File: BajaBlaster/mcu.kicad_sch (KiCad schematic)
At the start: 15 parts, among them J1 Conn_01x06_Socket, SW1 SW_Push, SW2 SW_Push, U1 ESP32-WROOM-32, U2 MPU-6050

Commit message: fixed one typographical error
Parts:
- C11: value .1uf -> 0.1uf
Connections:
- net CAN_RX: now also U1.10 (IO25); no longer U1.11 (IO26)
- net CAN_TX: now also U1.11 (IO26); no longer U1.10 (IO25)
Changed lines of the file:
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@@
 	(wire
 		(pts
-			(xy 83.82 88.9) (xy 80.01 88.9)
+			(xy 85.09 88.9) (xy 80.01 88.9)
 		)
 		(stroke
@@
 	(wire
 		(pts
-			(xy 83.82 86.36) (xy 80.01 86.36)
+			(xy 85.09 86.36) (xy 80.01 86.36)
 		)
 		(stroke
@@
 		)
 	)
-	(label "CAN_RX"
-		(at 83.82 88.9 0)
-		(effects
-			(font
-				(size 1.27 1.27)
-			)
-			(justify left bottom)
-		)
-	)
-	(label "CAN_TX"
-		(at 83.82 86.36 0)
-		(effects
-			(font
-				(size 1.27 1.27)
-			)
-			(justify left bottom)
-		)
-	)
 	(label "IMU_SDA"
 		(at 120.65 64.77 180)
@@
 		)
 	)
+	(hierarchical_label "CAN_TX"
+		(shape bidirectional)
+		(at 85.09 88.9 0)
+		(effects
+			(font
+				(size 1.27 1.27)
+			)
+			(justify left)
+		)
+	)
 	(hierarchical_label "IO1"
 		(shape bidirectional)
@@
 			)
 			(justify right)
+		)
+	)
+	(hierarchical_label "CAN_RX"
+		(shape bidirectional)
+		(at 85.09 86.36 0)
+		(effects
+			(font
+				(size 1.27 1.27)
+			)
+			(justify left)
 		)
 	)
@@
 			)
 		)
-		(property "Value" ".1uf"
+		(property "Value" "0.1uf"
 			(at 147.32 43.18 90)
 			(show_name no)

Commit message: doing lots of small tweaks and fixups
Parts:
- added R302: 50OHM, symbol Device:R
- C301: renamed from C6; value 1uf -> 1uF
- C302: renamed from C8; value 10uf -> 10uF
- C304: renamed from C11; value 0.1uf -> 0.1uF
- R303: renamed from R1; value 10k Ohm -> 10kOhm
- R304: renamed from R2; value 4.7k -> 4.7kOHM
- R305: renamed from R3; value 4.7k -> 4.7kOHM
- renumbered C7 to C303, C9 to C305, C10 to C306, J1 to J301, R4 to R301, SW1 to SW301, SW2 to SW302, U1 to U301, U2 to U302
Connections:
- net +3V3: now also R303.1; no longer R303.2
- net ESP32 EN: no longer C301.1, R301.2, SW301.1, U301.3 (EN)
- net IMU_SCL: no longer R305.1, U302.23 (SCL)
- net IMU_SDA: no longer R304.1, U302.24 (SDA)
- net IO0: now also R303.2; no longer R303.1
- net IO1: no longer U301.35 (TXD0/IO1)
- net IO3: no longer U301.34 (RXD0/IO3)
- net SYNC: now also R302.2; no longer U301.12 (IO27)
- new net: R304.1, U302.23 (SCL)
- new net: R305.1, U302.24 (SDA)
- new net: R302.1, U301.12 (IO27)
- new net ESP32_EN: C301.1, R301.2, SW301.1, U301.3 (EN)
- new net U0RXD: U301.34 (RXD0/IO3)
- new net U0TXD: U301.35 (TXD0/IO1)
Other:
- note added: "ACCELEROMETER UNIT"
- note added: "ESP32"
- note added: "TESTING PADS"
- title: (none) -> MCU_REV_A
- moved on the sheet: C301, C302, C303, C304, C305, C306, J301, R301, R303, R304, R305, SW301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

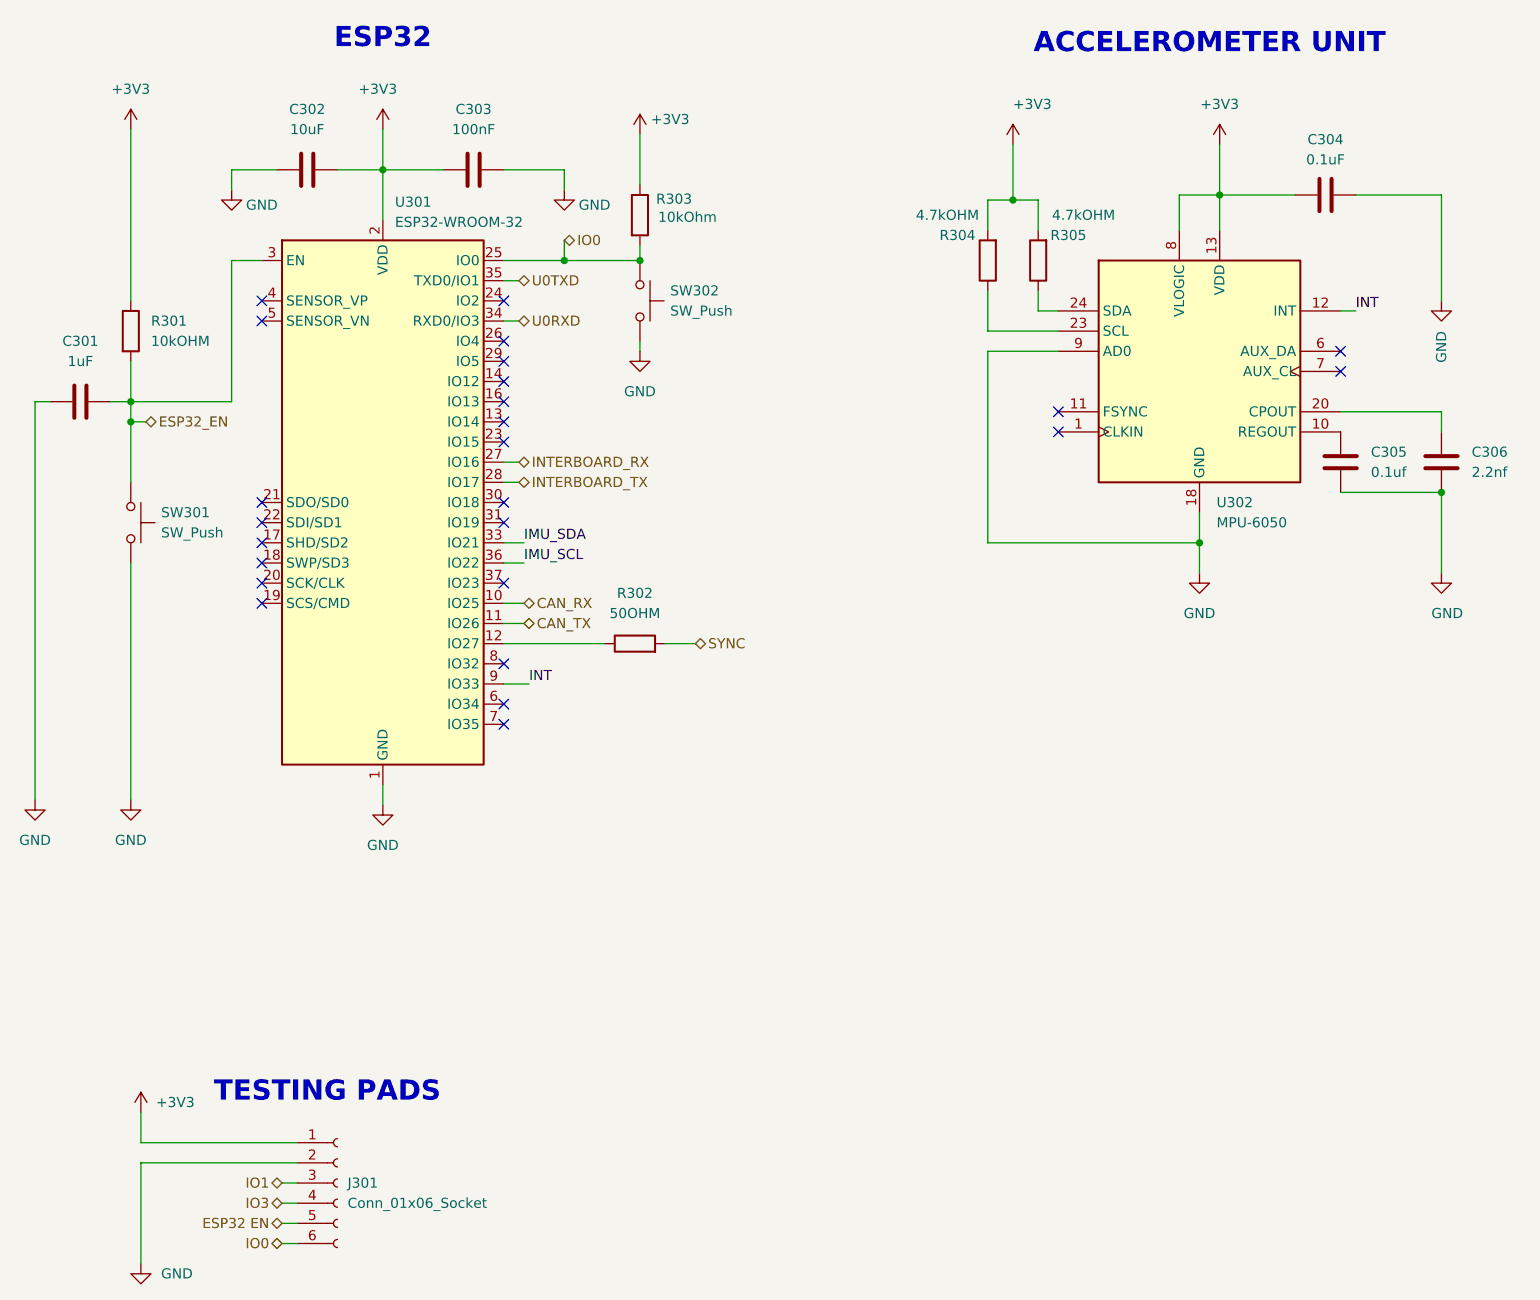
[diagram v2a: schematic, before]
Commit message: added better formatting across schematic
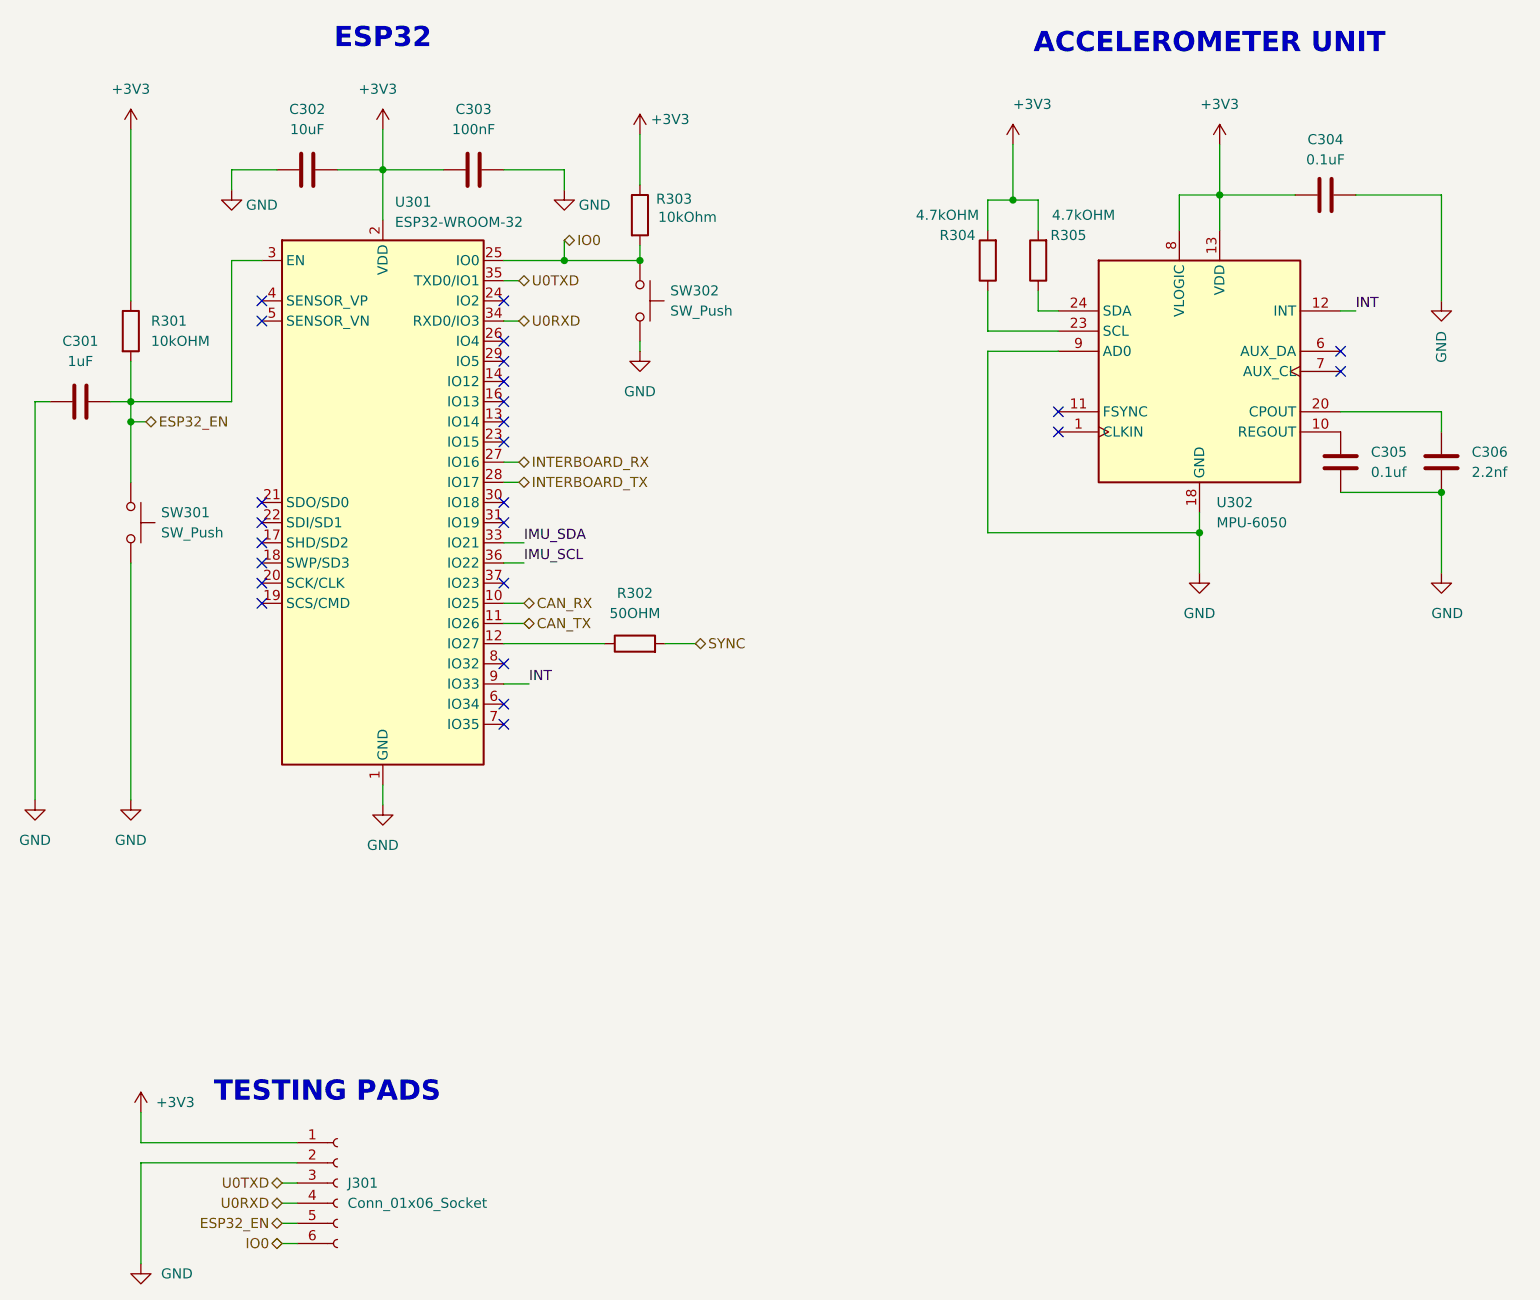
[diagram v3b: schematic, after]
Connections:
- net ESP32 EN is gone; now on net ESP32_EN: J301.5 (Pin_5)
- net IO1 is gone; now on net U0TXD: J301.3 (Pin_3)
- net IO3 is gone; now on net U0RXD: J301.4 (Pin_4)
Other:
- company: (none) -> Olin Baja SAE
- title: MCU_REV_A -> BAJA_BLASTER
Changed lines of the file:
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@@
 	(paper "A4")
 	(title_block
-		(title "MCU_REV_A")
+		(title "BAJA_BLASTER")
+		(date "2026-09-24")
+		(rev "A")
+		(company "Olin Baja SAE")
 	)
 	(text "ACCELEROMETER UNIT"
@@
 	)
 	(junction
-		(at 168.91 87.63)
-		(diameter 0)
-		(color 0 0 0 0)
-	)
-	(junction
 		(at 88.9 52.07)
 		(diameter 0)
@@
 	)
 	(junction
+		(at 168.91 86.36)
+		(diameter 0)
+		(color 0 0 0 0)
+	)
+	(junction
 		(at 34.29 72.39)
 		(diameter 0)
@@
 	(wire
 		(pts
-			(xy 168.91 83.82) (xy 168.91 87.63)
+			(xy 168.91 83.82) (xy 168.91 86.36)
 		)
 		(stroke
@@
 	(wire
 		(pts
+			(xy 168.91 86.36) (xy 168.91 91.44)
+		)
+		(stroke
+			(width 0)
+			(type default)
+		)
+	)
+	(wire
+		(pts
 			(xy 35.56 163.195) (xy 55.245 163.195)
 		)
@@
 	(wire
 		(pts
-			(xy 142.24 63.5) (xy 142.24 87.63)
-		)
-		(stroke
-			(width 0)
-			(type default)
-		)
-	)
-	(wire
-		(pts
-			(xy 142.24 87.63) (xy 168.91 87.63)
+			(xy 142.24 63.5) (xy 142.24 86.36)
+		)
+		(stroke
+			(width 0)
+			(type default)
+		)
+	)
+	(wire
+		(pts
+			(xy 142.24 86.36) (xy 168.91 86.36)
 		)
 		(stroke
@@
 		(pts
 			(xy 46.99 69.85) (xy 46.99 52.07)
-		)
-		(stroke
-			(width 0)
-			(type default)
-		)
-	)
-	(wire
-		(pts
-			(xy 168.91 87.63) (xy 168.91 91.44)
 		)
 		(stroke
@@
 		)
 	)
-	(hierarchical_label "ESP32 EN"
+	(hierarchical_label "ESP32_EN"
 		(shape bidirectional)
 		(at 53.34 173.355 180)
@@
 		)
 	)
-	(hierarchical_label "IO1"
+	(hierarchical_label "U0TXD"
 		(shape bidirectional)
 		(at 53.34 168.275 180)
@@
 		)
 	)
-	(hierarchical_label "IO3"
+	(hierarchical_label "U0RXD"
 		(shape bidirectional)
 		(at 53.34 170.815 180)

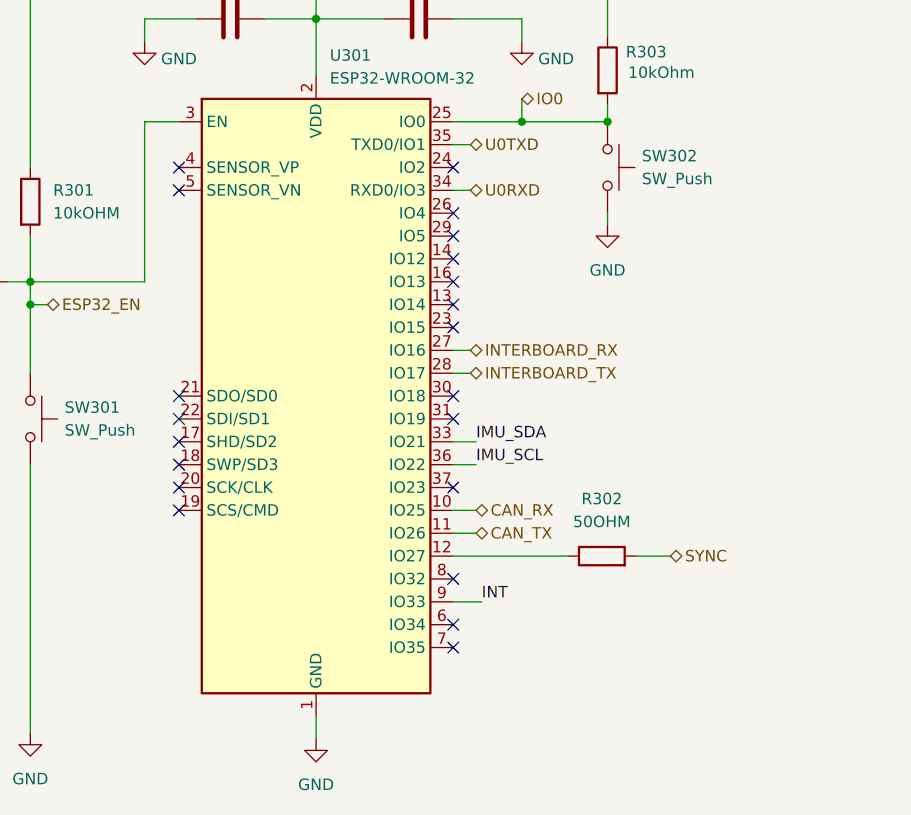
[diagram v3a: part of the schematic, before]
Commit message: working on adding footprints - about half done
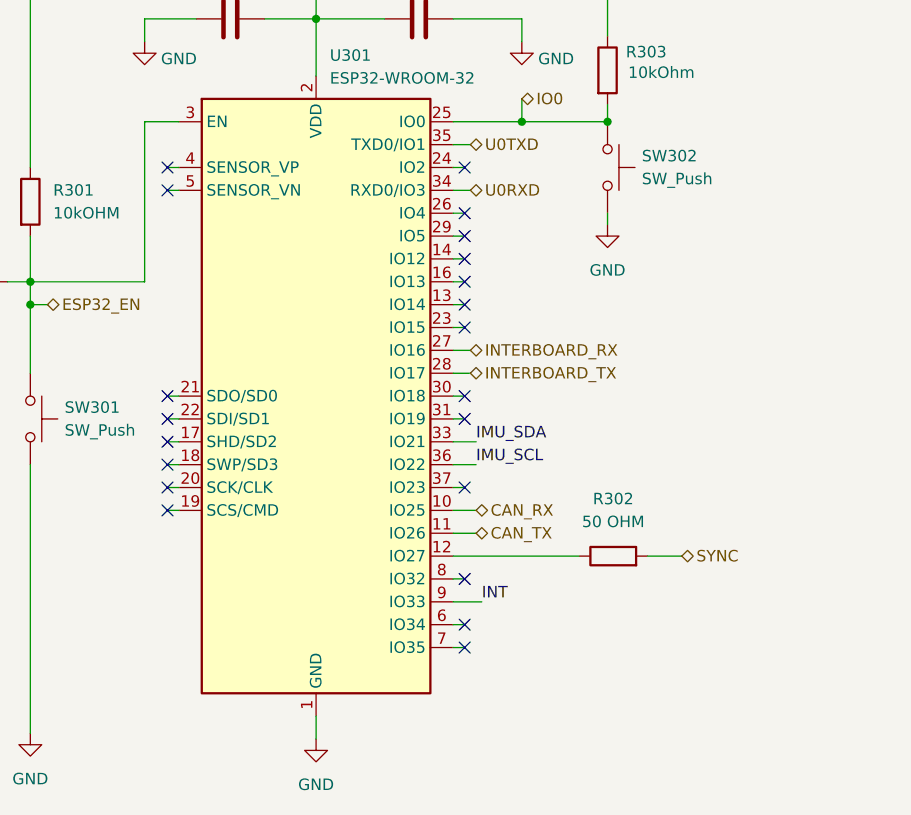
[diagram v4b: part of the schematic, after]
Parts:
- C302, C304, C305, C306: footprint Package_SO:SOIC-8_3.9x4.9mm_P1.27mm -> Capacitor_SMD:C_0805_2012Metric
- C303: footprint (none) -> Capacitor_SMD:C_0805_2012Metric
- R301: footprint (none) -> Resistor_SMD:R_0805_2012Metric
- R302: value 50OHM -> 50 OHM; footprint (none) -> Resistor_SMD:R_0805_2012Metric
- R303, R304, R305: footprint Package_DIP:DIP-8_W7.62mm -> Resistor_SMD:R_0805_2012Metric
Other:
- moved on the sheet: R302

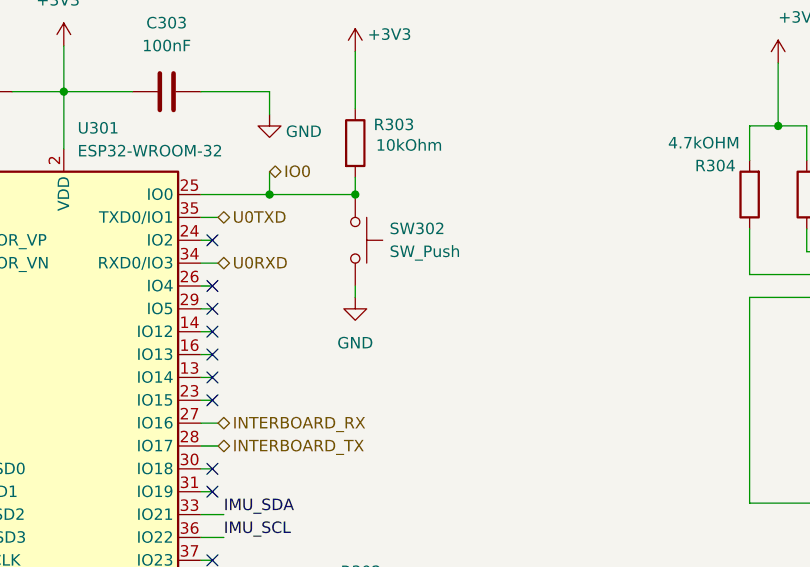
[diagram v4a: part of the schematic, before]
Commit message: added all the footprints - no errors - dont know if they are correct yet though
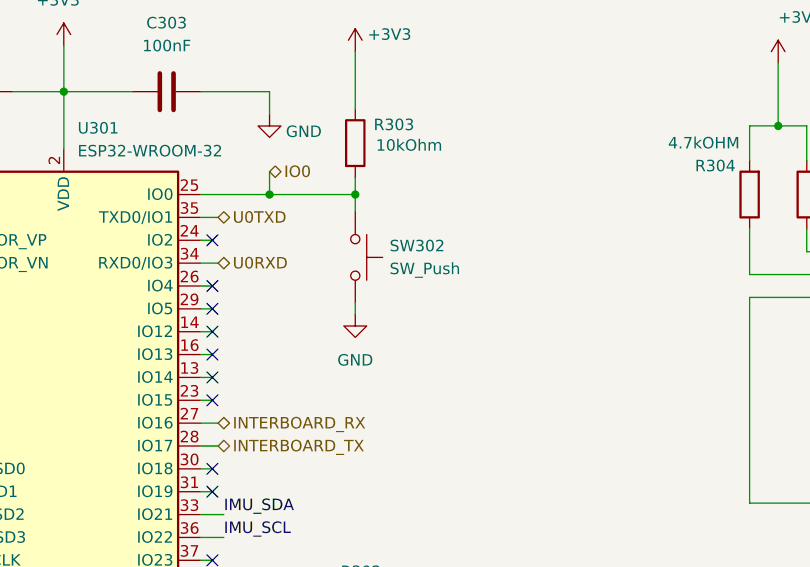
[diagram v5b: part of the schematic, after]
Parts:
- C301: footprint (none) -> Capacitor_SMD:C_0805_2012Metric
- SW301: footprint Package_DIP:DIP-24_W7.62mm -> Button_Switch_SMD:SW_SPST_TL3342
- SW302: footprint (none) -> Button_Switch_SMD:SW_SPST_TL3342
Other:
- moved on the sheet: SW302
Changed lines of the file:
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@@
 	(wire
 		(pts
-			(xy 98.425 63.5) (xy 98.425 62.23)
+			(xy 98.425 65.405) (xy 98.425 64.135)
 		)
 		(stroke
@@
 	(wire
 		(pts
+			(xy 98.425 53.975) (xy 98.425 52.07)
+		)
+		(stroke
+			(width 0)
+			(type default)
+		)
+	)
+	(wire
+		(pts
 			(xy 35.56 165.735) (xy 55.245 165.735)
 		)
@@
 	(symbol
 		(lib_id "power:GND")
-		(at 98.425 63.5 0)
+		(at 98.425 65.405 0)
 		(unit 1)
 		(body_style 1)
@@
 		(fields_autoplaced yes)
 		(property "Reference" "#PWR0311"
-			(at 98.425 69.85 0)
+			(at 98.425 71.755 0)
 			(hide yes)
 			(show_name no)
@@
 		)
 		(property "Value" "GND"
-			(at 98.425 68.58 0)
+			(at 98.425 70.485 0)
 			(show_name no)
 			(do_not_autoplace no)
@@
 		)
 		(property "Footprint" ""
-			(at 98.425 63.5 0)
+			(at 98.425 65.405 0)
 			(hide yes)
 			(show_name no)
@@
 		)
 		(property "Datasheet" ""
-			(at 98.425 63.5 0)
+			(at 98.425 65.405 0)
 			(hide yes)
 			(show_name no)
@@
 		)
 		(property "Description" "Power symbol creates a global label with name \"GND\" , ground"
-			(at 98.425 63.5 0)
+			(at 98.425 65.405 0)
 			(hide yes)
 			(show_name no)
@@
 			)
 		)
-		(property "Footprint" "Package_DIP:DIP-24_W7.62mm"
+		(property "Footprint" "Button_Switch_SMD:SW_SPST_TL3342"
 			(at 39.37 85.09 0)
 			(hide yes)
@@
 			)
 		)
-		(property "Footprint" ""
+		(property "Footprint" "Capacitor_SMD:C_0805_2012Metric"
 			(at 24.13 70.8152 0)
 			(hide yes)
@@
 	(symbol
 		(lib_id "Switch:SW_Push")
-		(at 98.425 57.15 270)
+		(at 98.425 59.055 270)
 		(unit 1)
 		(body_style 1)
@@
 		(fields_autoplaced yes)
 		(property "Reference" "SW302"
-			(at 102.235 55.8799 90)
+			(at 102.235 57.7849 90)
 			(show_name no)
 			(do_not_autoplace no)
@@
 		)
 		(property "Value" "SW_Push"
-			(at 102.235 58.4199 90)
+			(at 102.235 60.3249 90)
 			(show_name no)
 			(do_not_autoplace no)
@@
 			)
 		)
-		(property "Footprint" ""
-			(at 103.505 57.15 0)
+		(property "Footprint" "Button_Switch_SMD:SW_SPST_TL3342"
+			(at 103.505 59.055 0)
 			(hide yes)
 			(show_name no)
@@
 		)
 		(property "Datasheet" ""
-			(at 103.505 57.15 0)
+			(at 103.505 59.055 0)
 			(hide yes)
 			(show_name no)
@@
 		)
 		(property "Description" "Push button switch, generic, two pins"
-			(at 98.425 57.15 0)
+			(at 98.425 59.055 0)
 			(hide yes)
 			(show_name no)
